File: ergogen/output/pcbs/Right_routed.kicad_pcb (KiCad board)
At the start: 2 copper layers, 130.3 x 105.3 mm, 44 parts

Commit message: update config
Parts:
- MCU1: footprint 1:xiao_smd_xl_cutout -> 1:xiao_smd_xl_cutout_minimal
- SW1: footprint power_switch -> 1208YD
- moved SW1 58.6 mm to (262.2, 34.2), turned to 0 degrees
- moved S19 58.0 mm to (319.2, 31.4)
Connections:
- MCU1 pad 17: GND -> RST
- SW1 pad 1: (no net) -> BAT_CONN
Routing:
- net BAT_CONN: track 86.2 -> 151.4 mm
- net RST: track 86.9 -> 27.0 mm
- net GND: track 166.4 -> 108.9 mm
- net BAT: track 22.0 -> 70.8 mm, vias 1 -> 0
- net C4: track 169.2 -> 165.0 mm
- net mirror_extension_cluster: track 12.9 -> 14.1 mm
- net mirror_base_cluster: track 13.2 -> 14.2 mm
- net mirror_middle_top: track 12.9 -> 13.7 mm
- net C2: track 118.9 -> 118.1 mm
- net mirror_index_home: track 12.9 -> 13.6 mm
- net R3: track 184.5 -> 183.9 mm
- net R2: track 155.0 -> 154.3 mm
- net mirror_index_top: track 13.0 -> 13.7 mm
- net mirror_middle_home: track 13.0 -> 13.6 mm
- net C0: track 46.9 -> 47.4 mm
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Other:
- board size 130.3 x 105.3 mm -> 130 x 105 mm
- board text added: "liaison"
- board text removed: "JLCJLCJLCJLC"
- board text removed: "ON"
- board text removed: "alias"
- board text removed: "v2"

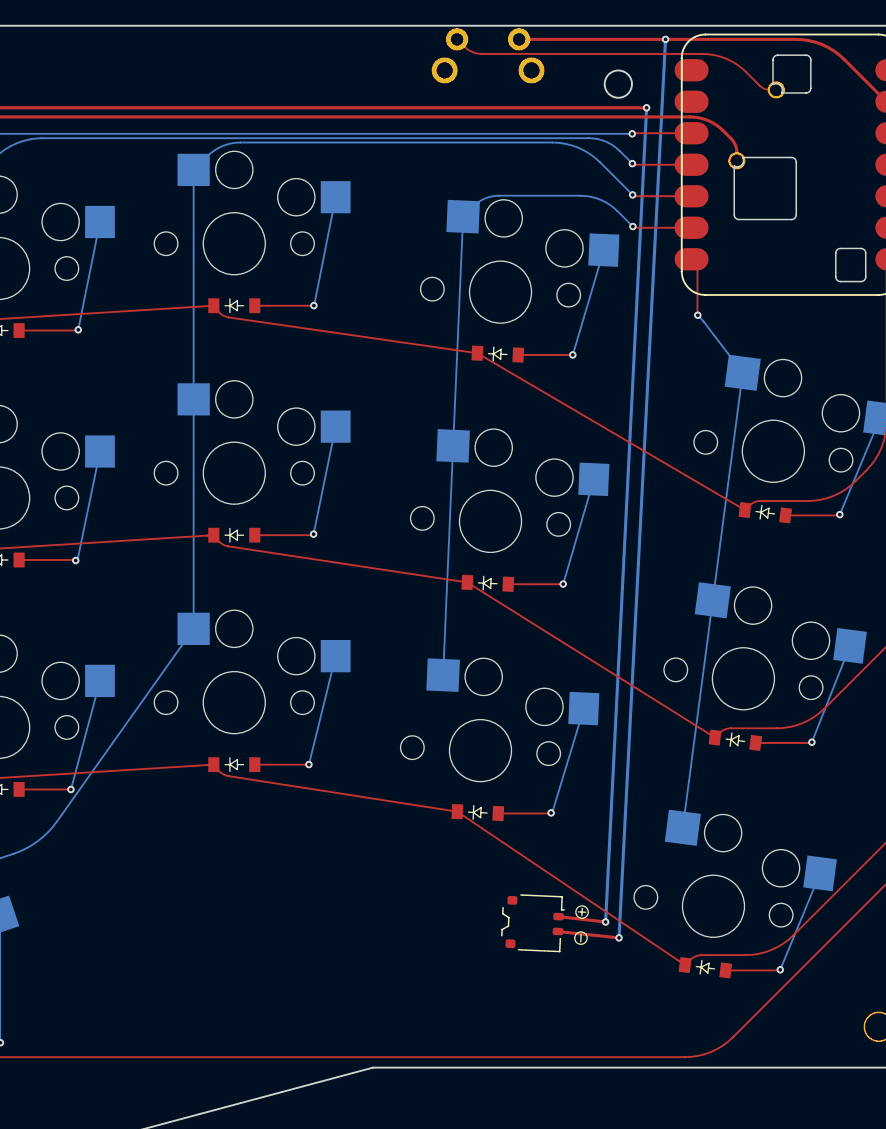
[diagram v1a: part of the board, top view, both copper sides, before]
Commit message: add battery outlines to pcb
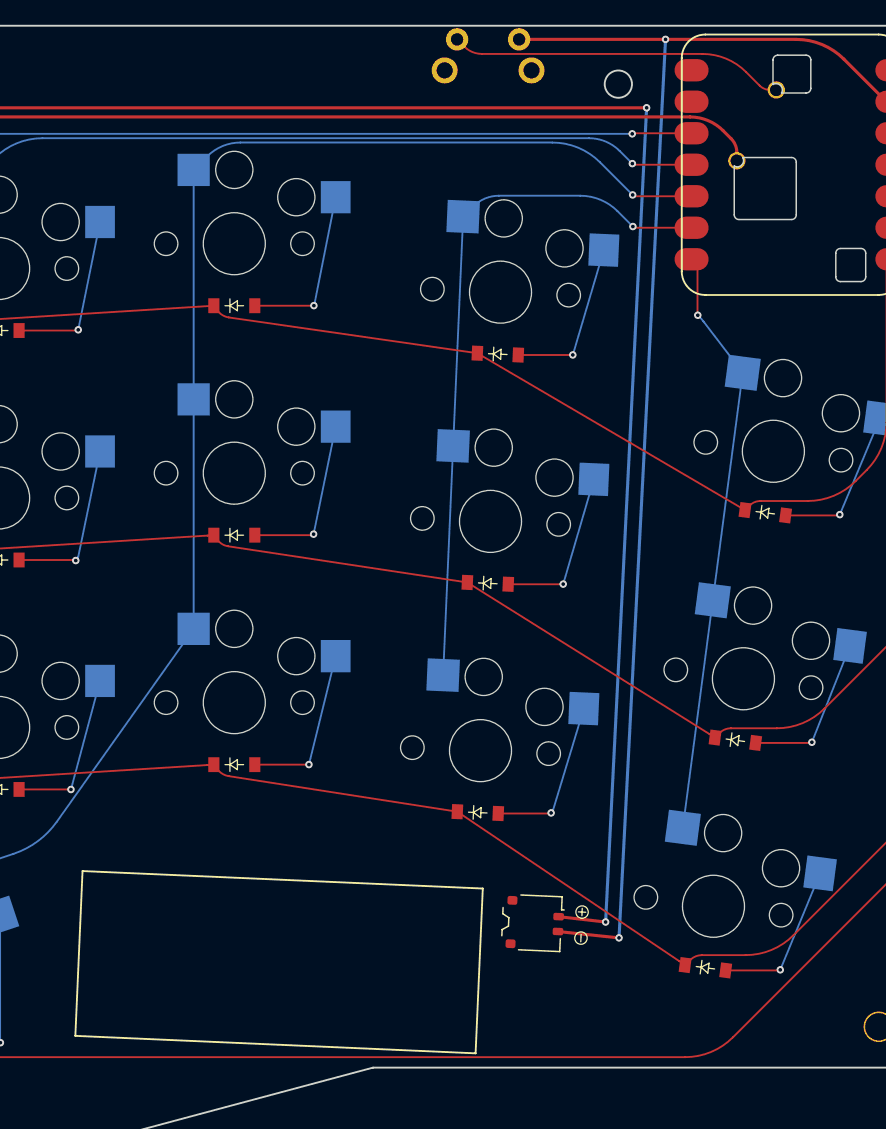
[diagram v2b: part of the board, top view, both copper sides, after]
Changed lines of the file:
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@@
 		(fp_arc
 			(start 1.136553 -8.832047)
-			(mid 1.405961 -8.720454)
+			(mid 1.405958 -8.720453)
 			(end 1.517553 -8.451047)
 			(stroke
@@
 		)
 	)
+	(gr_line
+		(start 318.16116 111.857809)
+		(end 318.741297 98.570467)
+		(stroke
+			(width 0.15)
+			(type default)
+		)
+		(layer "F.SilkS")
+	)
+	(gr_line
+		(start 285.891902 110.448903)
+		(end 318.16116 111.857809)
+		(stroke
+			(width 0.15)
+			(type default)
+		)
+		(layer "F.SilkS")
+	)
+	(gr_line
+		(start 286.47204 97.161561)
+		(end 285.891902 110.448903)
+		(stroke
+			(width 0.15)
+			(type default)
+		)
+		(layer "F.SilkS")
+	)
+	(gr_line
+		(start 318.741297 98.570467)
+		(end 286.47204 97.161561)
+		(stroke
+			(width 0.15)
+			(type default)
+		)
+		(layer "F.SilkS")
+	)
 	(gr_arc
 		(start 224.747353 112.712095)
@@
 		)
 	)
+	(group ""
+		(members "4b99118d-87c3-4402-8d22-bcfc277e6c65" "9a8c711a-ec1b-4ae9-a23b-6d37e016581a"
+			"bbe822da-0266-4750-b4f6-0c60f285cf28" "f717c276-7fe2-4483-babc-28ec5259f045"
+		)
+	)
